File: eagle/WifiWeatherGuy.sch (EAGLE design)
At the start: 3 parts

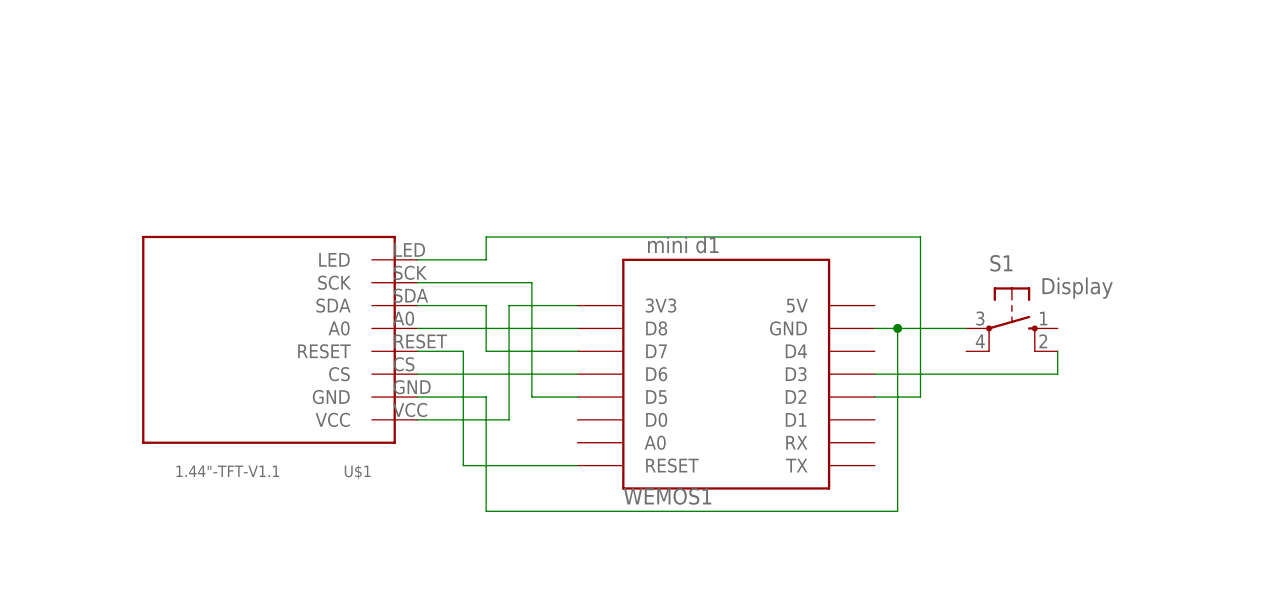
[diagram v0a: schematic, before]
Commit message: add wemos pin headers
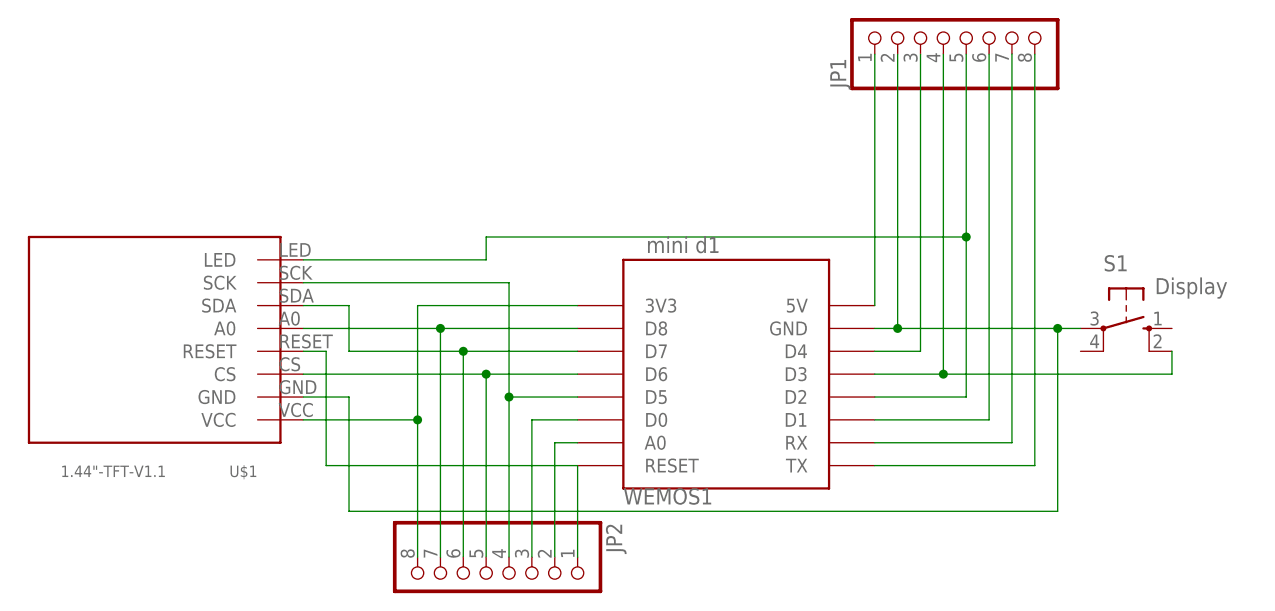
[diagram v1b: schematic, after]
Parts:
- added JP1, JP2: (no value), pinhead:PINHD-1X8
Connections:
- new net N$10: JP1.1, WEMOS1.5V
- new net N$11: JP1.3, WEMOS1.D4
- new net N$12: JP1.6, WEMOS1.D1
- new net N$13: JP1.7, WEMOS1.RX
- new net N$14: JP1.8, WEMOS1.TX
- new net N$15: JP2.2, WEMOS1.A0
- new net N$16: JP1.2, S1.P, U$1.GND, WEMOS1.GND
- net N$1: now also JP2.8
- net N$2: now also JP2.5
- net N$3: now also JP2.7
- net N$4: now also JP2.6
- net N$5: now also JP2.4
- net N$6: now also JP1.5
- net N$7: now also JP2.3, WEMOS1.D0; no longer S1.P, U$1.GND, WEMOS1.GND
- net N$8: now also JP2.1
- net N$9: now also JP1.4
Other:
- moved on the sheet: S1, U$1
